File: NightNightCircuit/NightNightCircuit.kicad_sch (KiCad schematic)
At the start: 9 parts, among them M1 Motor_Servo, U1 XIAO ESP32C3, U2 DS3231M, U3 TPS61022

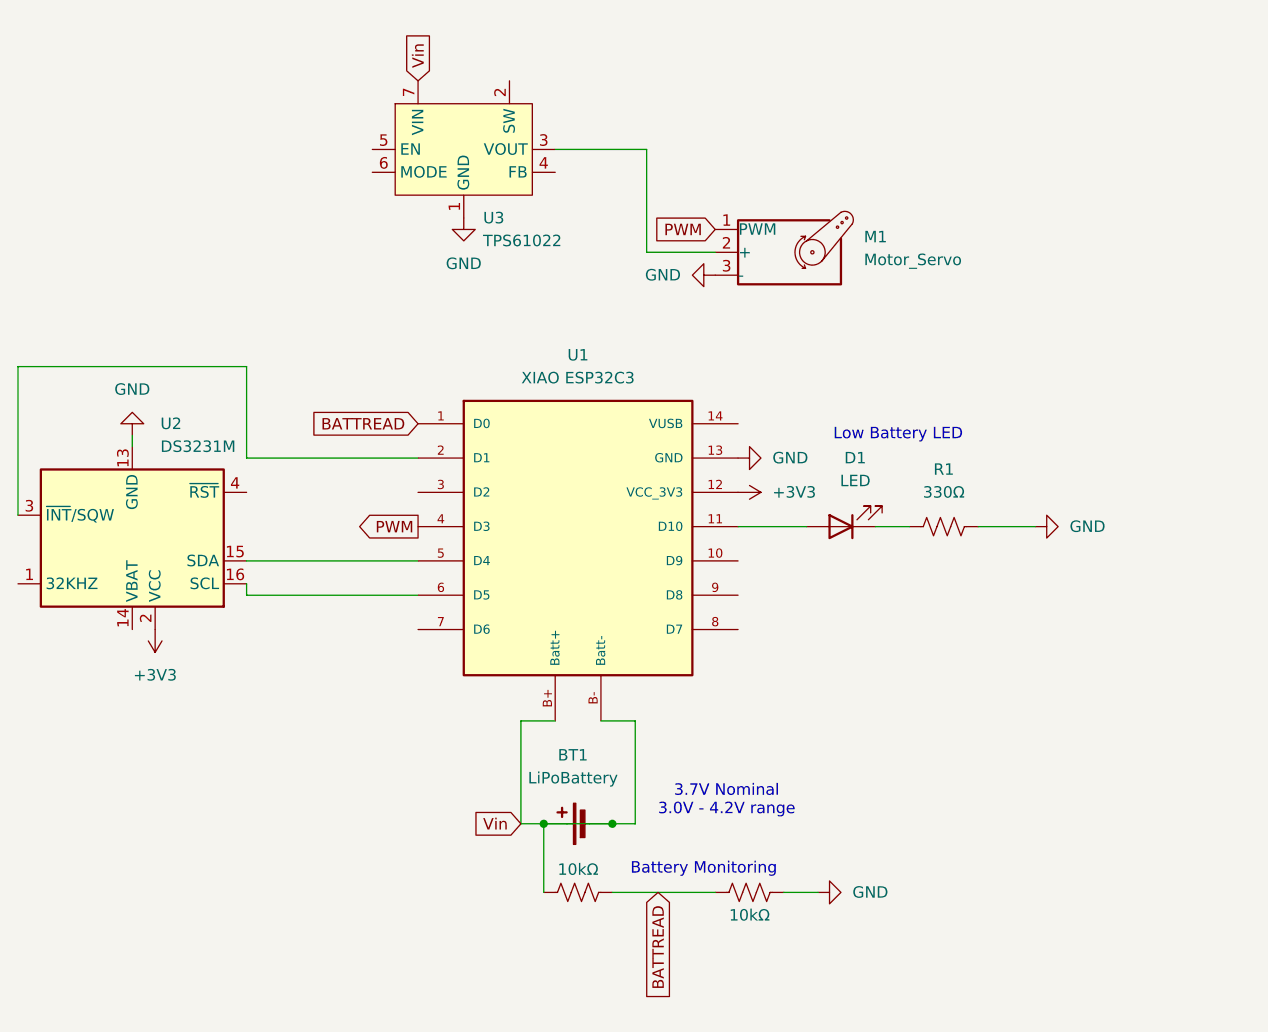
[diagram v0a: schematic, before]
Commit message: Fixed rtc-actuator test, circuit diagram, and main code
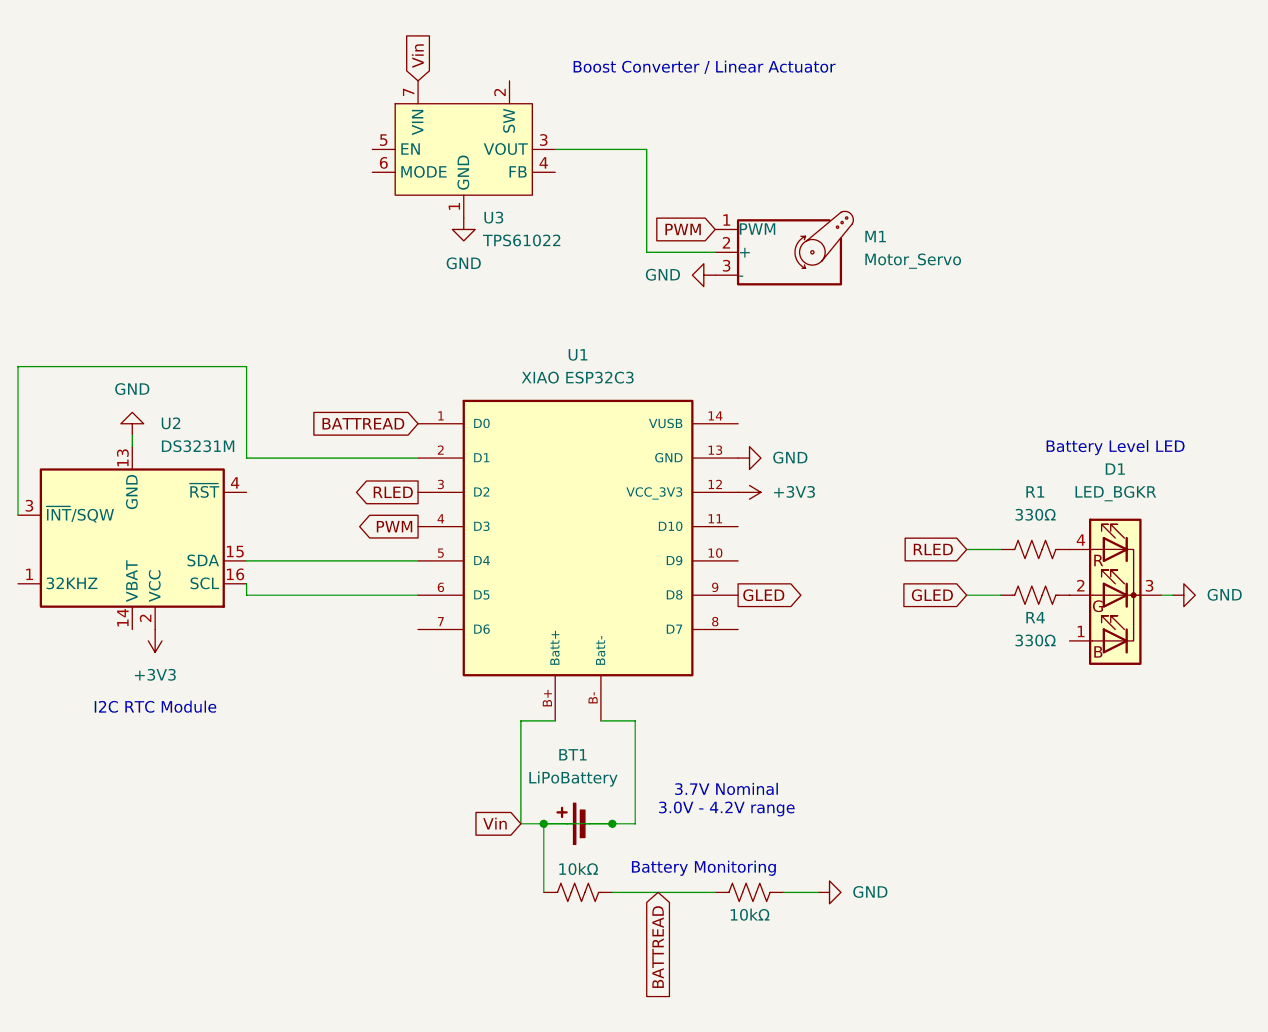
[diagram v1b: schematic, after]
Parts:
- removed D1: LED, symbol Device:LED
- added D1: LED_BGKR, symbol Device:LED_BGKR
- added R4: 330Ω, symbol Device:R_US
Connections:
- net GND: now also D1.3 (K); no longer R1.2
- net RLED: now reaches R1.1
- net RLED: now also U1.3 (D2)
- net GLED: now reaches U1.9 (D8)
- net GLED: now also R4.1
- new net: D1.4 (RA), R1.2
- new net: D1.2 (GA), R4.2
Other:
- note added: "Battery Level LED"
- note added: "Boost Converter / Linear Actuator"
- note added: "I2C RTC Module"
- note removed: "Low Battery LED"
- moved on the sheet: R1
